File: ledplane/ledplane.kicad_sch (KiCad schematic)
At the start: 41 parts

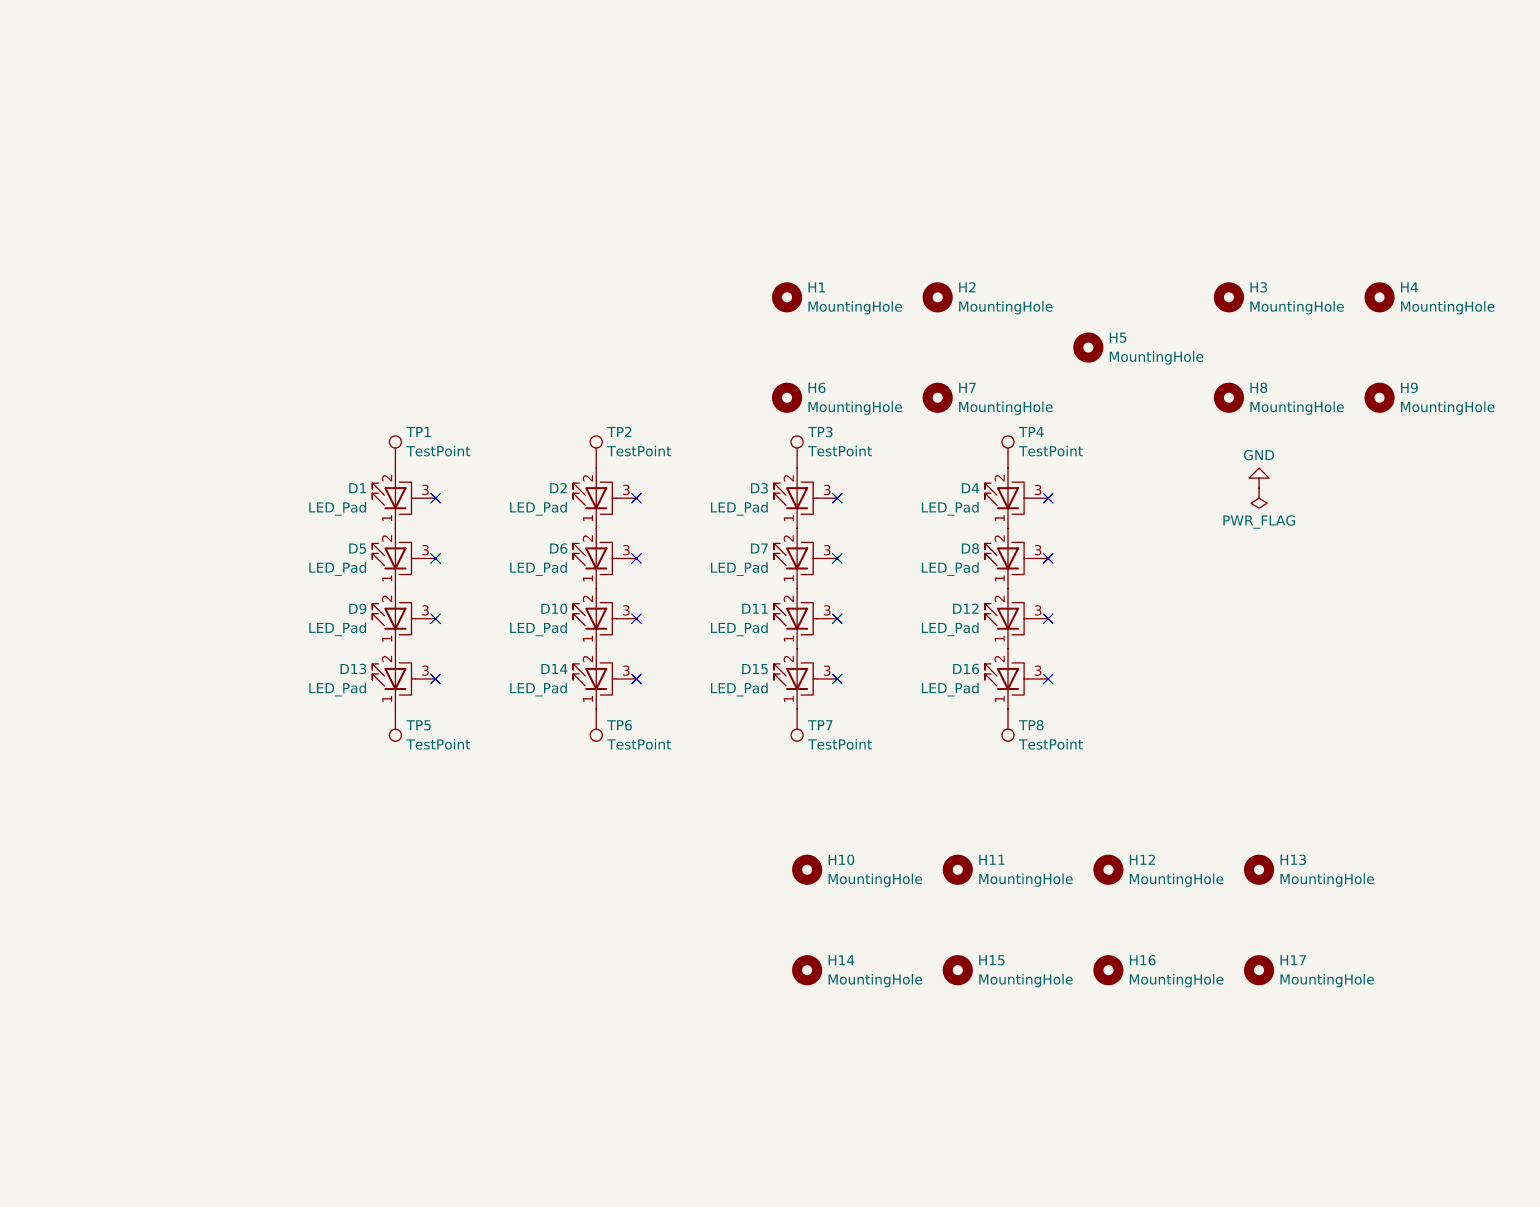
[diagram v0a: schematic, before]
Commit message: Update LED plane to be all in series
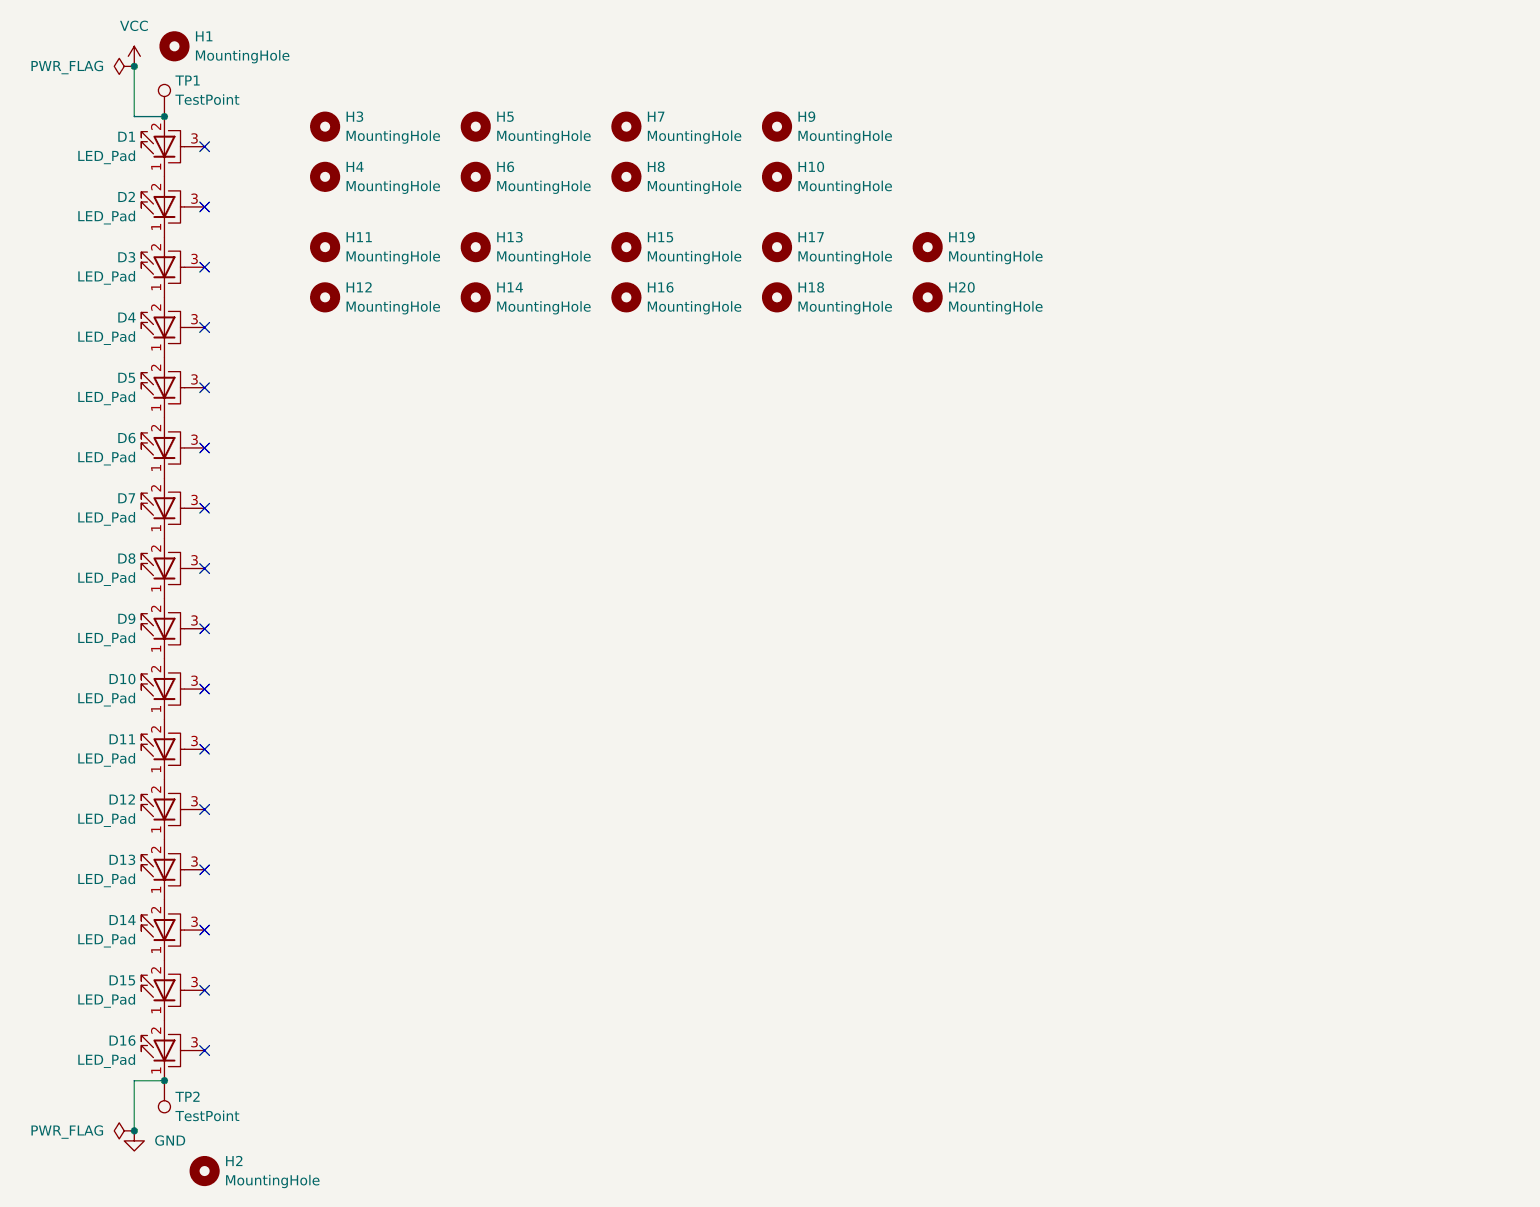
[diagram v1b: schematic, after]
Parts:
- removed H10, H6, H7, H9: MountingHole, MountingHole:MountingHole_2.2mm_M2, symbol Mechanical:MountingHole
- removed TP2, TP3, TP4, TP5, TP6, TP7: TestPoint, misc:SolderWirePad_1x01_SMD_4x6mm, symbol Connector:TestPoint
- added H12, H14, H15, H17, H18, H19, H20: MountingHole, MountingHole:MountingHole_3.2mm_M3, symbol Mechanical:MountingHole
- H10: renamed from H4; footprint MountingHole:MountingHole_2.2mm_M2 -> MountingHole:MountingHole_3.2mm_M3
- H11: renamed from H12; footprint MountingHole:MountingHole_2.2mm_M2 -> MountingHole:MountingHole_3.2mm_M3
- H13, H16: footprint MountingHole:MountingHole_2.2mm_M2 -> MountingHole:MountingHole_3.2mm_M3
- H3: renamed from H1; footprint MountingHole:MountingHole_2.2mm_M2 -> MountingHole:MountingHole_3.2mm_M3
- H4: renamed from H14; footprint MountingHole:MountingHole_2.2mm_M2 -> MountingHole:MountingHole_3.2mm_M3
- H5: renamed from H2; footprint MountingHole:MountingHole_2.2mm_M2 -> MountingHole:MountingHole_3.2mm_M3
- H6: renamed from H11; footprint MountingHole:MountingHole_2.2mm_M2 -> MountingHole:MountingHole_3.2mm_M3
- H7: renamed from H15; footprint MountingHole:MountingHole_2.2mm_M2 -> MountingHole:MountingHole_3.2mm_M3
- H8: renamed from H5; footprint MountingHole:MountingHole_2.2mm_M2 -> MountingHole:MountingHole_3.2mm_M3
- H9: renamed from H8; footprint MountingHole:MountingHole_2.2mm_M2 -> MountingHole:MountingHole_3.2mm_M3
- renumbered D7 to D10, D15 to D12, D4 to D13, D8 to D14, D12 to D15, D5 to D2, D9 to D3, D13 to D4, D2 to D5, D10 to D7, D14 to D8, D3 to D9, H3 to H1, H17 to H2, TP8 to TP2
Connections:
- net GND: now also D16.1 (K), TP2.1
- net at D12.1 (K): now also D13.2 (A)
- net VCC: now reaches D1.2 (A), TP1.1
- net at D4.1 (K): now also D5.2 (A)
- net at D9.2 (A): now also D8.1 (K)
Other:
- moved on the sheet: D1, D10, D11, D12, D13, D14, D15, D16, D2, D3, D4, D5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
